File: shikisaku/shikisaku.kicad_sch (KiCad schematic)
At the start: 6 parts, among them J1 HC-SR04, J2 HC-SR04, SW1 SW_Reset, SW2 SW_Push, U1 ProMicro, U2 MMC5603

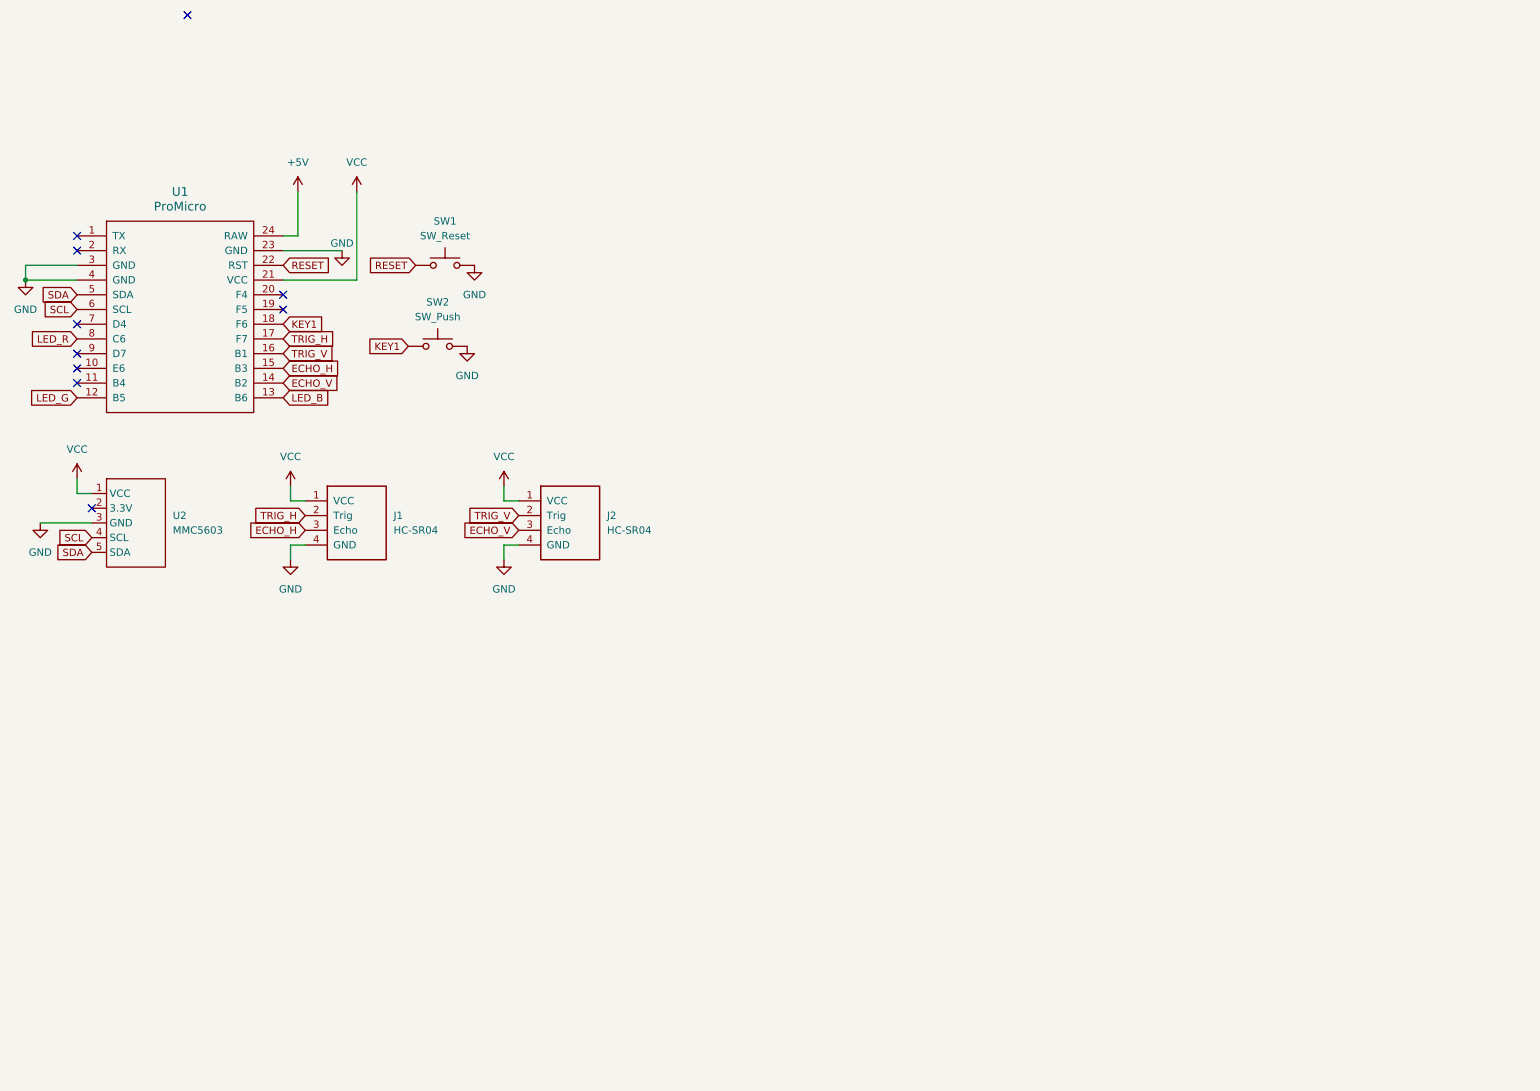
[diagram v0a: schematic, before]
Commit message: update schematic
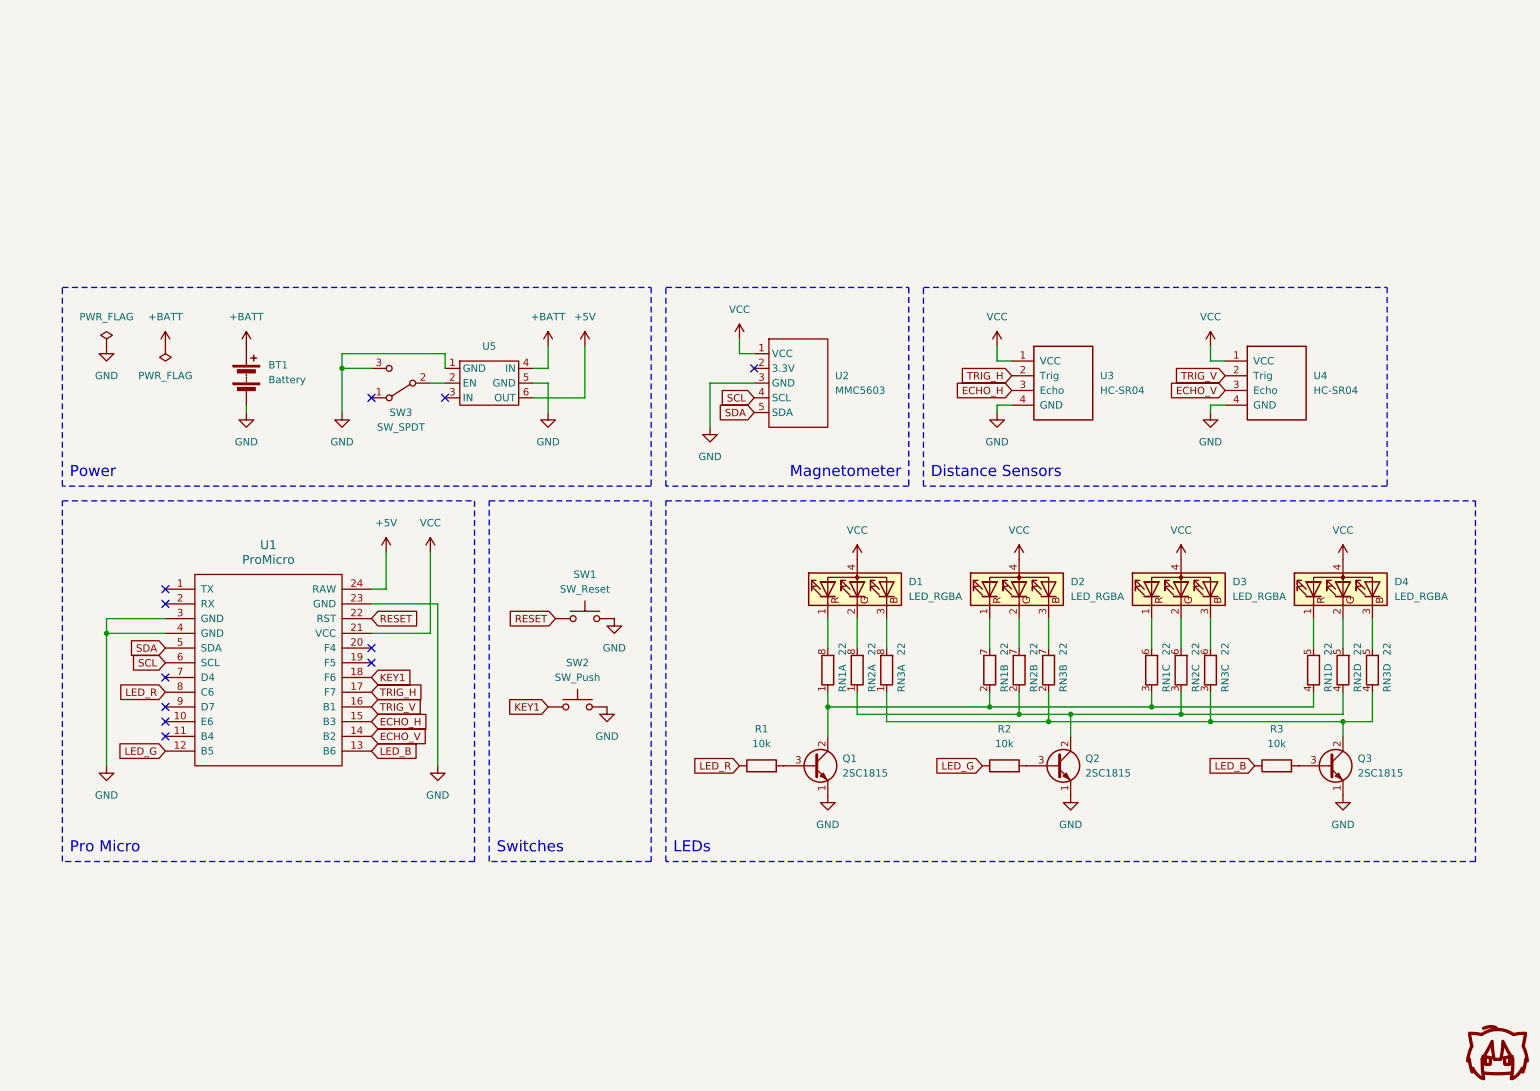
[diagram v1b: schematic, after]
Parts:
- added BT1: Battery, symbol Device:Battery
- added D1, D2, D3, D4: LED_RGBA, symbol Device:LED_RGBA
- added Q1, Q2, Q3: 2SC1815, Package_TO_SOT_THT:TO-92_Inline, symbol Transistor_BJT:2SC1815
- added R1, R2, R3: 10k, symbol Device:R
- added RN1, RN2, RN3: 22, symbol Device:R_Pack04_Split
- added SW3: SW_SPDT, symbol Switch:SW_SPDT
- added U5: ~, symbol akizuki:XCL103
- renumbered J1 to U3, J2 to U4
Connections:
- net +5V: now also U5.6 (OUT)
- net GND: now also BT1.2 (-), Q1.1 (E), Q2.1 (E), Q3.1 (E), SW3.3 (C), U5.1 (GND), U5.5 (GND)
- net LED_B: now also R3.1
- net LED_G: now also R2.1
- net LED_R: now also R1.1
- net VCC: now also D1.4 (A), D2.4 (A), D3.4 (A), D4.4 (A)
- new net: Q1.2 (C), RN1.1 (R1.1), RN1.2 (R2.1), RN1.3 (R3.1), RN1.4 (R4.1)
- new net: D1.1 (RK), RN1.8 (R1.2)
- new net: D2.1 (RK), RN1.7 (R2.2)
- new net: D1.2 (GK), RN2.8 (R1.2)
- new net: D1.3 (BK), RN3.8 (R1.2)
- new net: Q3.2 (C), RN3.1 (R1.1), RN3.2 (R2.1), RN3.3 (R3.1), RN3.4 (R4.1)
- new net: Q3.3 (B), R3.2
- new net: Q2.2 (C), RN2.1 (R1.1), RN2.2 (R2.1), RN2.3 (R3.1), RN2.4 (R4.1)
- new net: D3.1 (RK), RN1.6 (R3.2)
- new net: D3.3 (BK), RN3.6 (R3.2)
- new net: SW3.2 (B), U5.2 (EN)
- new net: Q2.3 (B), R2.2
- new net: D4.1 (RK), RN1.5 (R4.2)
- new net: D4.2 (GK), RN2.5 (R4.2)
- new net: D4.3 (BK), RN3.5 (R4.2)
- new net: Q1.3 (B), R1.2
- new net: D3.2 (GK), RN2.6 (R3.2)
- new net: D2.2 (GK), RN2.7 (R2.2)
- new net: D2.3 (BK), RN3.7 (R2.2)
- new net +BATT: BT1.1 (+), U5.4 (IN)
- no-connect marks 10 -> 11
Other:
- note added: "Distance Sensors"
- note added: "LEDs"
- note added: "Magnetometer"
- note added: "Power"
- note added: "Pro Micro"
- note added: "Switches"
- moved on the sheet: SW1, SW2, U1, U2, U3, U4

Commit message: assign footprints
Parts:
- removed SW3: SW_SPDT, symbol Switch:SW_SPDT
- removed U3, U4: HC-SR04, symbol Connector_Generic:Conn_01x04
- added SW3: SW_SPST, Connector_JST:JST_XH_B2B-XH-A_1x02_P2.50mm_Vertical, symbol Switch:SW_SPST
- added U3, U4: HC-SR04, Connector_JST:JST_XH_B4B-XH-A_1x04_P2.50mm_Vertical, symbol akizuki:HC-SR04
- BT1: value Battery -> 3.6V; footprint (none) -> Connector_JST:JST_XH_B2B-XH-A_1x02_P2.50mm_Vertical
- D1, D2, D3, D4: footprint (none) -> akizuki:LED_OSTBMAZ2C1D
- R1, R2, R3: footprint (none) -> Resistor_THT:R_Axial_DIN0207_L6.3mm_D2.5mm_P7.62mm_Horizontal
- RN1, RN2, RN3: footprint (none) -> Resistor_SMD:R_Array_Convex_4x0603_1
- SW1: footprint (none) -> Button_Switch_THT:SW_PUSH_1P1T_6x3.5mm_H4.3_APEM_MJTP1243
- SW2: footprint (none) -> Connector_JST:JST_XH_B2B-XH-A_1x02_P2.50mm_Vertical
- U1: footprint (none) -> promicro:ProMicro
- U2: footprint (none) -> Adafruit:MMC5603
- U5: value ~ -> XCL103; footprint (none) -> akizuki:XCL103
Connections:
- net +5V: now also U5.4 (OUT); no longer U5.6 (OUT)
- net +BATT: now also U5.6 (IN); no longer U5.4 (IN)
- net ECHO_H: now also U3.3 (Echo)
- net ECHO_V: now also U4.3 (Echo)
- net GND: now also SW3.1 (A), U3.4 (GND), U4.4 (GND)
- net TRIG_H: now also U3.2 (Trig)
- net TRIG_V: now also U4.2 (Trig)
- net VCC: now also D1.1 (A), D2.1 (A), D3.1 (A), D4.1 (A), U3.1 (VCC), U4.1 (VCC); no longer D1.4 (A), D2.4 (A), D3.4 (A), D4.4 (A)
- net at RN1.8 (R1.2): now also D1.4 (RK); no longer D1.1 (RK)
- net at RN1.7 (R2.2): now also D2.4 (RK); no longer D2.1 (RK)
- net at D1.2 (BK): now also RN3.8 (R1.2); no longer RN2.8 (R1.2)
- net at D1.3 (GK): now also RN2.8 (R1.2); no longer RN3.8 (R1.2)
- net at RN1.6 (R3.2): now also D3.4 (RK); no longer D3.1 (RK)
- net at RN3.6 (R3.2): now also D3.2 (BK); no longer D3.3 (BK)
- net at U5.2 (EN): now also SW3.2 (B)
- net at RN1.5 (R4.2): now also D4.4 (RK); no longer D4.1 (RK)
- net at D4.2 (BK): now also RN3.5 (R4.2); no longer RN2.5 (R4.2)
- net at D4.3 (GK): now also RN2.5 (R4.2); no longer RN3.5 (R4.2)
- net at RN2.6 (R3.2): now also D3.3 (GK); no longer D3.2 (GK)
- net at RN2.7 (R2.2): now also D2.3 (GK); no longer D2.2 (GK)
- net at RN3.7 (R2.2): now also D2.2 (BK); no longer D2.3 (BK)
- no-connect marks 11 -> 10
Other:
- moved on the sheet: U5

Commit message: layout footprints
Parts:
- BT1: footprint Connector_JST:JST_XH_B2B-XH-A_1x02_P2.50mm_Vertical -> Connector_JST:JST_XH_S2B-XH-A_1x02_P2.50mm_Horizontal
- U1: footprint promicro:ProMicro -> promicro:ProMicro-EnforcedTop
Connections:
- net ECHO_H: now also U1.16 (B1); no longer U1.15 (B3)
- net TRIG_V: now also U1.15 (B3); no longer U1.16 (B1)
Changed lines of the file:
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@@
     )
   )
-  (global_label "ECHO_H" (shape input) (at 81.28 116.84 0) (fields_autoplaced)
+  (global_label "ECHO_H" (shape input) (at 81.28 114.3 0) (fields_autoplaced)
     (effects (font (size 1.27 1.27)) (justify left))
-    (property "Intersheetrefs" "${INTERSHEET_REFS}" (at 91.6433 116.84 0)
+    (property "Intersheetrefs" "${INTERSHEET_REFS}" (at 91.6433 114.3 0)
       (effects (font (size 1.27 1.27)) (justify left) hide)
     )
@@
     )
   )
-  (global_label "TRIG_V" (shape input) (at 81.28 114.3 0) (fields_autoplaced)
+  (global_label "TRIG_V" (shape input) (at 81.28 116.84 0) (fields_autoplaced)
     (effects (font (size 1.27 1.27)) (justify left))
-    (property "Intersheetrefs" "${INTERSHEET_REFS}" (at 90.4338 114.3 0)
+    (property "Intersheetrefs" "${INTERSHEET_REFS}" (at 90.4338 116.84 0)
       (effects (font (size 1.27 1.27)) (justify left) hide)
     )
@@
       (effects (font (size 1.524 1.524)))
     )
-    (property "Footprint" "promicro:ProMicro" (at 66.04 139.7 0)
+    (property "Footprint" "promicro:ProMicro-EnforcedTop" (at 66.04 139.7 0)
       (effects (font (size 1.524 1.524)) hide)
     )
@@
       (effects (font (size 1.27 1.27)) (justify left))
     )
-    (property "Footprint" "Connector_JST:JST_XH_B2B-XH-A_1x02_P2.50mm_Vertical" (at 59.69 55.626 90)
-      (effects (font (size 1.27 1.27)) hide)
-    )
+    (property "Footprint" "Connector_JST:JST_XH_S2B-XH-A_1x02_P2.50mm_Horizontal" (at 59.69 55.626 90)
+      (effects (font (size 1.27 1.27)) hide)
+    )

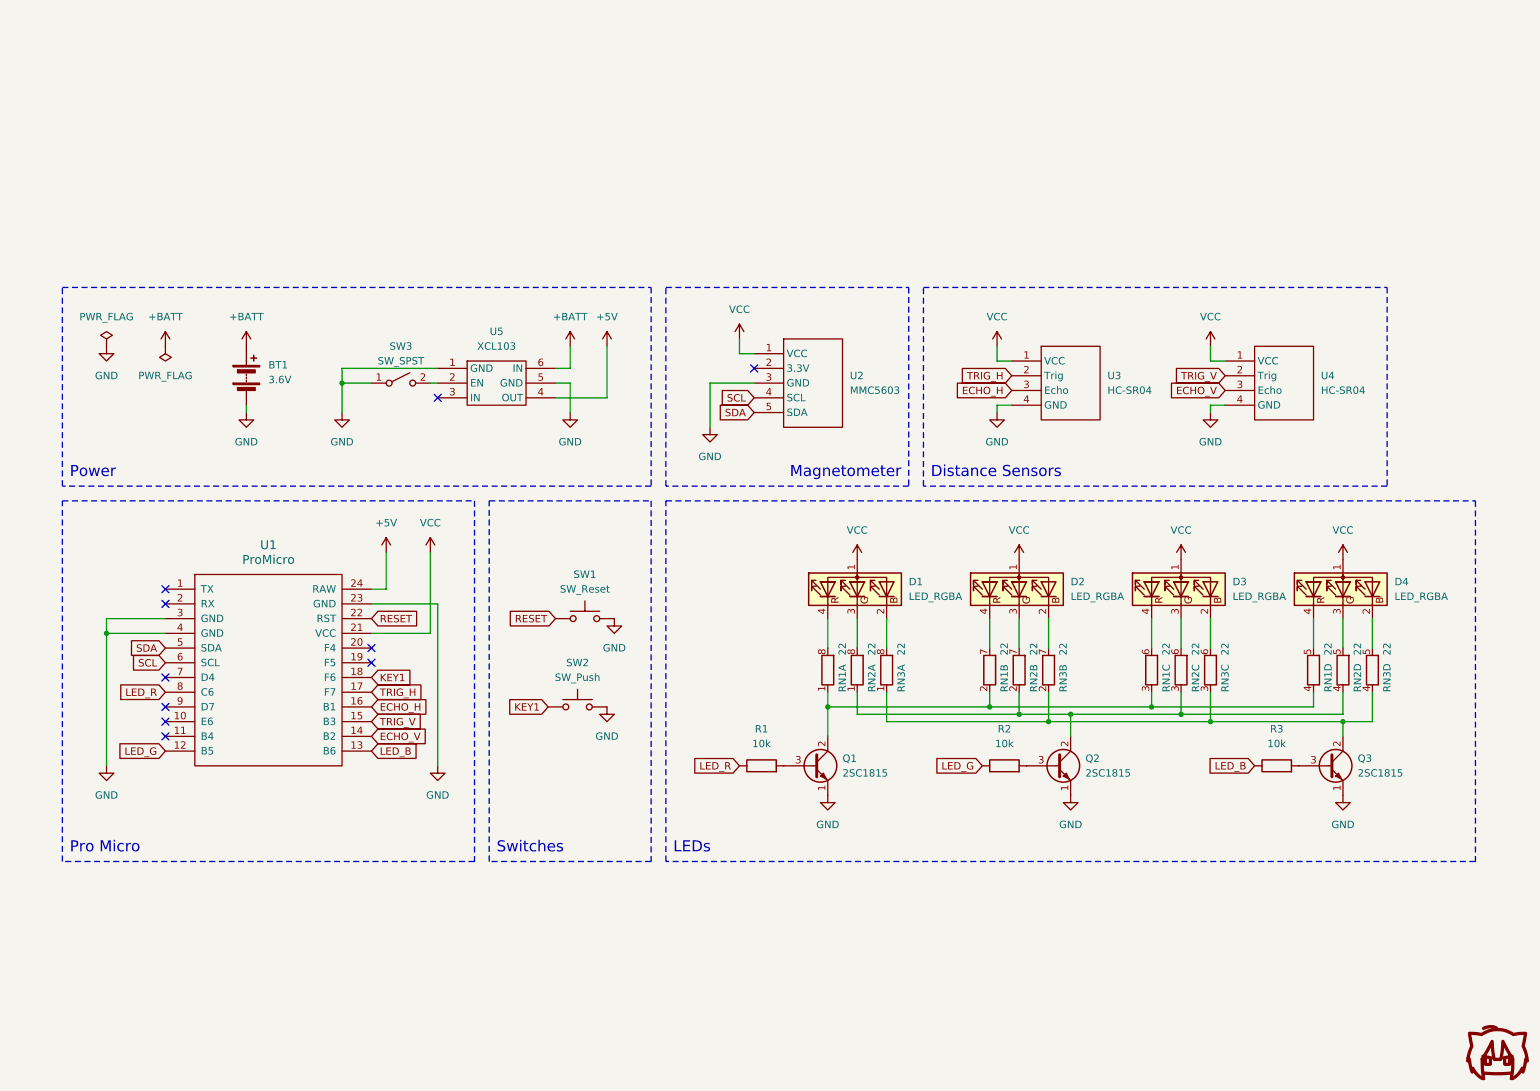
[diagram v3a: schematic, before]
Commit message: use SK6812MINI-E
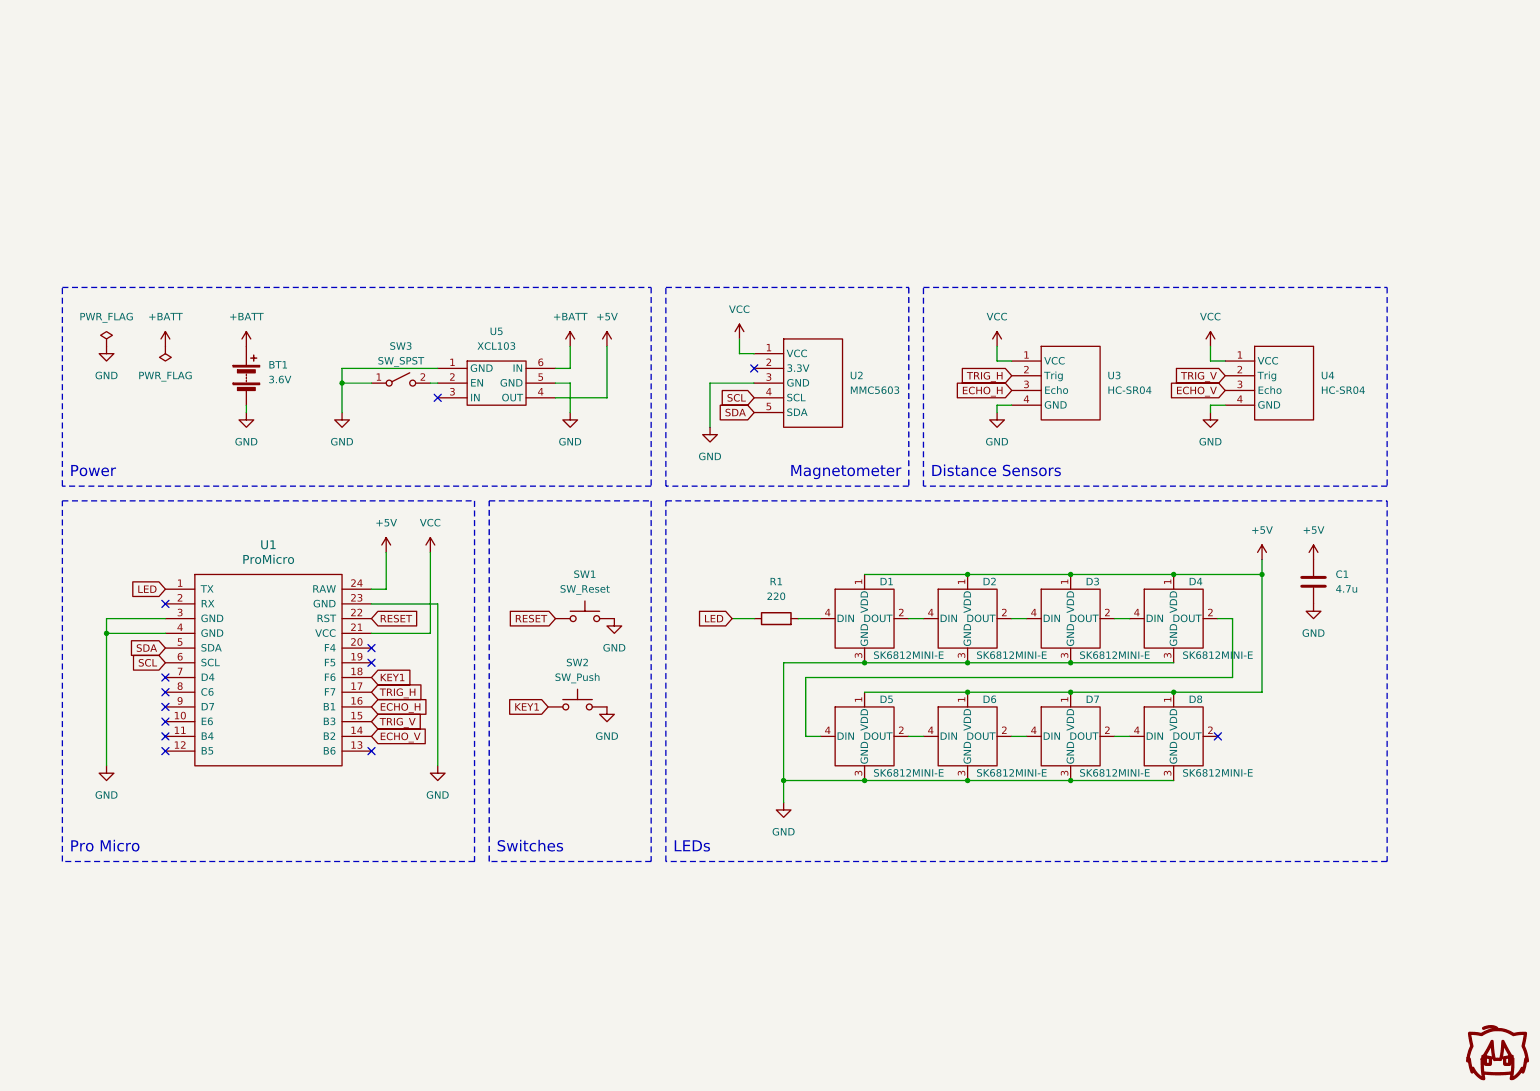
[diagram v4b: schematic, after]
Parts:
- removed D1, D2, D3, D4: LED_RGBA, akizuki:LED_OSTBMAZ2C1D, symbol Device:LED_RGBA
- removed Q1, Q2, Q3: 2SC1815, Package_TO_SOT_THT:TO-92_Inline, symbol Transistor_BJT:2SC1815
- removed R2, R3: 10k, Resistor_THT:R_Axial_DIN0207_L6.3mm_D2.5mm_P7.62mm_Horizontal, symbol Device:R
- removed RN1, RN2, RN3: 22, Resistor_SMD:R_Array_Convex_4x0603_1, symbol Device:R_Pack04_Split
- added C1: 4.7u, Capacitor_SMD:C_0805_2012Metric_Pad1.18x1.45mm_HandSolder, symbol Device:C
- added D1, D2, D3, D4, D5, D6, D7, D8: SK6812MINI-E, LED_SMD:LED_SK6812MINI-E, symbol LED:SK6812MINI-E
- R1: value 10k -> 220
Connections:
- net +5V: now also C1.1, D1.1 (VDD), D2.1 (VDD), D3.1 (VDD), D4.1 (VDD), D5.1 (VDD), D6.1 (VDD), D7.1 (VDD), D8.1 (VDD)
- net GND: now also C1.2, D1.3 (GND), D2.3 (GND), D3.3 (GND), D4.3 (GND), D5.3 (GND), D6.3 (GND), D7.3 (GND), D8.3 (GND)
- net at R1.2: now also D1.4 (DIN)
- net LED: now reaches U1.1 (TX)
- net LED: now also R1.1
- net LED_B: no longer names the net of U1.13 (B6)
- net LED_G: no longer names the net of U1.12 (B5)
- net LED_R: no longer names the net of U1.8 (C6)
- net LED_R: no longer R1.1
- new net: D2.2 (DOUT), D3.4 (DIN)
- new net: D1.2 (DOUT), D2.4 (DIN)
- new net: D3.2 (DOUT), D4.4 (DIN)
- new net: D7.2 (DOUT), D8.4 (DIN)
- new net: D4.2 (DOUT), D5.4 (DIN)
- new net: D6.2 (DOUT), D7.4 (DIN)
- new net: D5.2 (DOUT), D6.4 (DIN)
- no-connect marks 10 -> 13
